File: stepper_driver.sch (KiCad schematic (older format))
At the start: 51 parts, among them IC1 TMC2590-TA-Trinamic, J1 BARREL_JACK, J2 Screw_Terminal_01x04, J3 CONN_01X14, J9 USB_C_Receptacle_USB2.0, Q1 Q_NPN_BEC, Q2 NCE4614, Q3 NCE4614, Q4 Q_NPN_BEC, Q5 NCE4614, Q6 NCE4614, SW1 SW_Push, U1 CH340G, U2 XC6210B332MR, U3 XL1509-5.0, U4 ESP32-WROOM-32, U6 SN74LV1T34DBV, Y1 12MHz

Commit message: Added PCB v1
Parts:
- C8: value 1uF/50V -> 1uF; footprint Capacitor_SMD:C_0603_1608Metric -> Capacitor_SMD:C_0402_1005Metric; LCSC C15849 -> C52923
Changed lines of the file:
@@
 Wire Wire Line
 	5200 1800 5350 1800
-Text Label 6700 1800 0    50   ~ 0
+Text Label 6700 1800 0    60   ~ 0
 IO0
 Wire Wire Line
@@
 Wire Wire Line
 	1050 8450 1050 8350
-$Comp
-L Device:C C8
-U 1 1 61C15625
-P 1050 8850
-F 0 "C8" H 1165 8896 50  0000 L CNN
-F 1 "1uF/50V" H 900 8750 50  0000 L CNN
-F 2 "Capacitor_SMD:C_0603_1608Metric" H 1088 8700 50  0001 C CNN
-F 3 "~" H 1050 8850 50  0001 C CNN
-F 4 "C15849" H 1050 8850 50  0001 C CNN "LCSC"
-	1    1050 8850
-	1    0    0    -1
-$EndComp
 Wire Wire Line
 	1050 8700 1050 8650
@@
 Text Label 5300 7950 2    50   ~ 0
 I39
-Text Label 6700 4000 0    50   ~ 0
+Text Label 6700 4000 0    60   ~ 0
 I34
-Text Label 6700 4100 0    50   ~ 0
+Text Label 6700 4100 0    60   ~ 0
 I35
 Text Label 5300 8050 2    50   ~ 0
@@
 Text Label 5300 8150 2    50   ~ 0
 I35
-Text Label 6700 3800 0    50   ~ 0
+Text Label 6700 3800 0    60   ~ 0
 IO32
-Text Label 6700 3900 0    50   ~ 0
+Text Label 6700 3900 0    60   ~ 0
 IO33
 Text Label 5300 8250 2    50   ~ 0
@@
 Wire Wire Line
 	5150 7750 5300 7750
-Text Label 6700 2500 0    50   ~ 0
+Text Label 6700 2500 0    60   ~ 0
 IO13
-Text Label 6700 3300 0    50   ~ 0
+Text Label 6700 3300 0    60   ~ 0
 IO22
 Text Label 5300 8450 2    50   ~ 0
 IO22
-Text Label 6700 2800 0    50   ~ 0
+Text Label 6700 2800 0    60   ~ 0
 IO16
-Text Label 6700 2900 0    50   ~ 0
+Text Label 6700 2900 0    60   ~ 0
 IO17
 Wire Wire Line
@@
 Text Label 5300 8550 2    50   ~ 0
 IO17
-Text Label 6700 2000 0    50   ~ 0
+Text Label 6700 2000 0    60   ~ 0
 IO2
-Text Label 6700 2700 0    50   ~ 0
+Text Label 6700 2700 0    60   ~ 0
 IO15
 Text Label 5300 8750 2    50   ~ 0
@@
 	1    0    0    -1
 $EndComp
+$Comp
+L Device:C C?
+U 1 1 617F308D
+P 1050 8850
+AR Path="/5F1ED570/617F308D" Ref="C?"  Part="1"
+AR Path="/617F308D" Ref="C8"  Part="1"
+F 0 "C8" H 950 8950 50  0000 L CNN
+F 1 "1uF" H 850 8750 50  0000 L CNN
+F 2 "Capacitor_SMD:C_0402_1005Metric" H 1088 8700 50  0001 C CNN
+F 3 "~" H 1050 8850 50  0001 C CNN
+F 4 "C52923" H 1050 8850 50  0001 C CNN "LCSC"
+	1    1050 8850
+	1    0    0    -1
+$EndComp

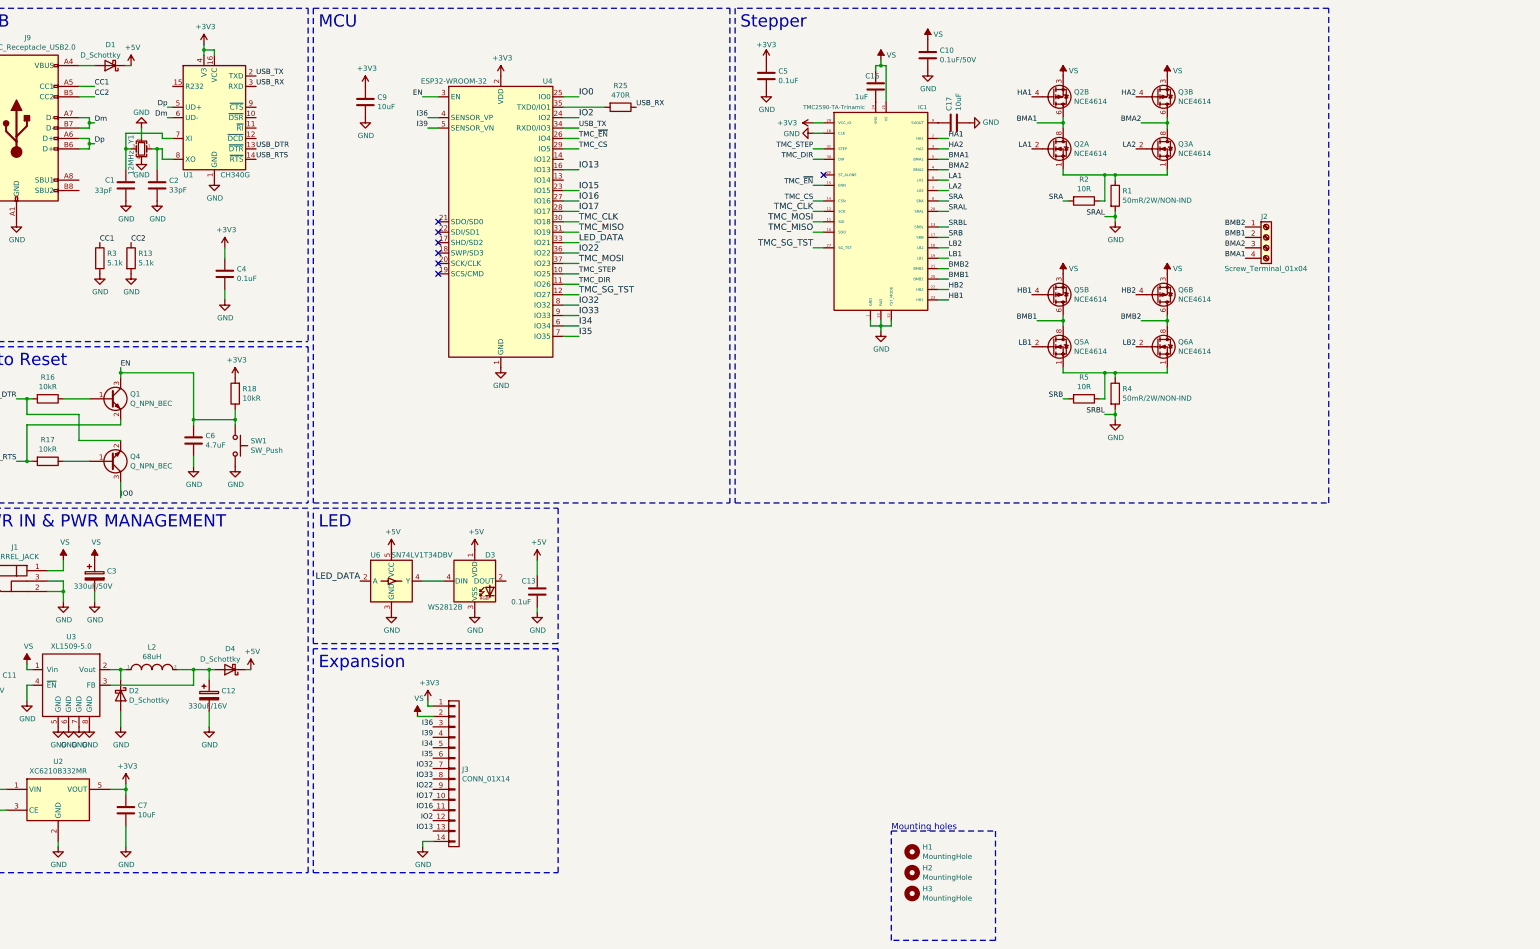
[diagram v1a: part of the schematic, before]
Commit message: Hardware design v2 with TMC2160 driver and NEMA 23 form factor for mounting
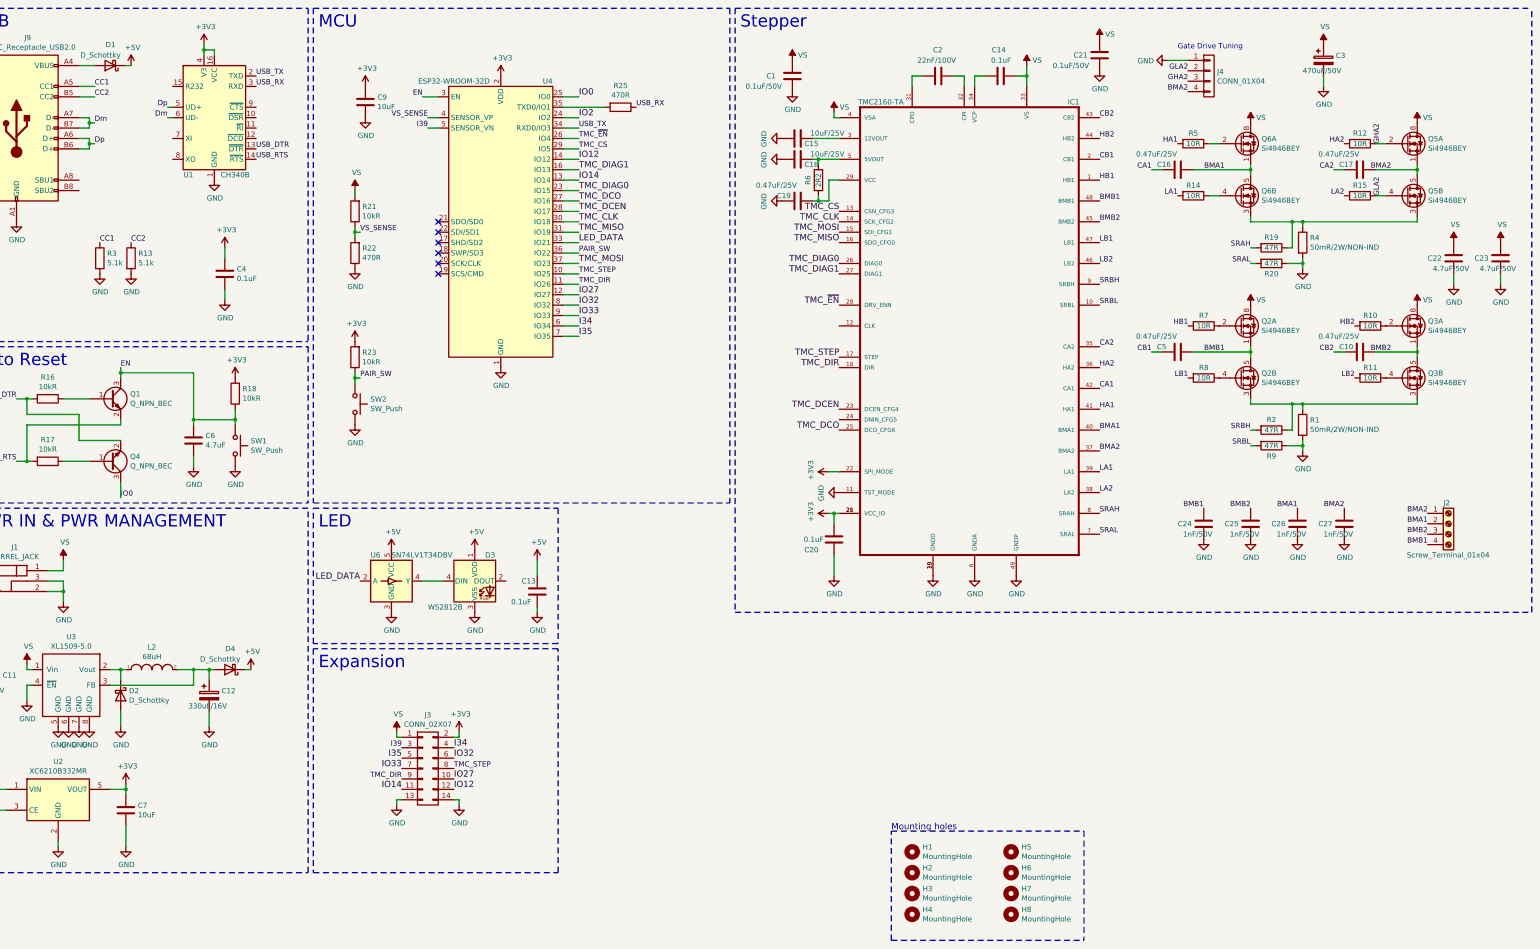
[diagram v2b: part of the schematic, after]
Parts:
- removed IC1: TMC2590-TA-Trinamic, TMC2590-eval:TQFP32-5x5mm, symbol tmc2590-ta-trinamic:TMC2590-TA-Trinamic
- removed J3: CONN_01X14, Connector_PinHeader_2.54mm:PinHeader_1x14_P2.54mm_Vertical, symbol conn1:CONN_01X14
- removed Q2, Q3, Q5, Q6: NCE4614, Package_SO:SOIC-8_3.9x4.9mm_P1.27mm, symbol Transistor_FET:IRF7309IPBF
- removed Y1: 12MHz, Crystal:Crystal_SMD_2520-4Pin_2.5x2.0mm, symbol Device:Crystal_GND24_Small
- added C14, C20: 0.1uF, Capacitor_SMD:C_0402_1005Metric, symbol Device:C
- added C15, C18: 10uF/25V, Capacitor_SMD:C_0603_1608Metric, symbol Device:C
- added C19: 0.47uF/25V, Capacitor_SMD:C_0402_1005Metric, symbol Device:C
- added C21: 0.1uF/50V, Capacitor_SMD:C_0603_1608Metric, symbol Device:C
- added C22, C23: 4.7uF/50V, Capacitor_SMD:C_0805_2012Metric, symbol Device:C
- added C24, C25, C26, C27: 1nF/50V, Capacitor_SMD:C_0402_1005Metric, symbol Device:C
- added H4, H5, H6, H7, H8: MountingHole, MountingHole:MountingHole_3.5mm, symbol Mechanical:MountingHole
- added IC1: TMC2160-TA, Package_QFP:LQFP-48-1EP_7x7mm_P0.5mm_EP3.6x3.6mm_ThermalVias, symbol TMC2160-TA:TMC2160-TA
- added J3: CONN_02X07, Connector_PinHeader_2.54mm:PinHeader_2x07_P2.54mm_Vertical, symbol conn1:CONN_02X07
- added J4: CONN_01X04, Connector_PinHeader_1.27mm:PinHeader_1x04_P1.27mm_Vertical, symbol conn1:CONN_01X04
- added Q2, Q3, Q5, Q6: Si4946BEY, Package_SO:SOIC-8_3.9x4.9mm_P1.27mm, symbol Transistor_FET:FDS6890A
- added R10, R11, R12, R14, R15, R7, R8: 10R, Resistor_SMD:R_0402_1005Metric, symbol Device:R
- added R19, R20, R9: 47R, Resistor_SMD:R_0402_1005Metric, symbol Device:R
- added R21, R23: 10kR, Resistor_SMD:R_0402_1005Metric, symbol Device:R
- added R22: 470R, Resistor_SMD:R_0402_1005Metric, symbol Device:R
- added R6: 2R2, Resistor_SMD:R_0402_1005Metric, symbol Device:R
- added SW2: SW_Push, Switch:SW_Push_1P1T_NO_5.1x5.1mm, symbol Switch:SW_Push
- C1: value 33pF -> 0.1uF/50V; footprint Capacitor_SMD:C_0402_1005Metric -> Capacitor_SMD:C_0603_1608Metric; LCSC C1562 -> C14663
- C10: value 0.1uF/50V -> 0.47uF/25V; footprint Capacitor_SMD:C_0603_1608Metric -> Capacitor_SMD:C_0402_1005Metric; LCSC C14663 -> C437527
- C16: value 1uF -> 0.47uF/25V; LCSC C52923 -> C437527
- C17: value 10uF -> 0.47uF/25V; LCSC C15525 -> C437527
- C2: value 33pF -> 22nF/100V; footprint Capacitor_SMD:C_0402_1005Metric -> Capacitor_SMD:C_0603_1608Metric; LCSC C1562 -> C342519
- C3: value 330uF/50V -> 470uF/50V; LCSC C88733 -> C106526
- C5: value 0.1uF -> 0.47uF/25V; LCSC C1525 -> C437527
- H1, H2, H3: footprint MountingHole:MountingHole_3.2mm_M3 -> MountingHole:MountingHole_3.5mm
- J2: footprint TerminalBlock_Phoenix:TerminalBlock_Phoenix_MPT-0,5-4-2.54_1x04_P2.54mm_Horizontal -> cixi_kefa_screw_terminals:KF2EDGR-3.81-4P; LCSC C474922 -> C441184
- R2: value 10R -> 47R; LCSC C25077 -> C25118
- U1: value CH340G -> CH340B; LCSC C14267 -> C81010
- U4: value ESP32-WROOM-32 -> ESP32-WROOM-32D; LCSC C82899 -> C473012
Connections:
- net SRB is gone; now on net HA1: R5.2
- net +3V3: now also C20.2, IC1.20 (VCC_IO), IC1.21 (VCC_IO), IC1.22 (SPI_MODE), J3.2 (P2), R23.2; no longer C5.1
- net BMA1: now also C16.1, J2.2 (Pin_2), C26.1, IC1.40 (BMA1), Q6.1 (S1), Q6.5 (D2), Q6.6 (D2); no longer J2.4 (Pin_4)
- net BMA2: now also C17.1, J2.1 (Pin_1), C27.1, IC1.37 (BMA2), J4.4 (P4), Q5.1 (S1), Q5.5 (D2), Q5.6 (D2); no longer J2.3 (Pin_3)
- net BMB1: now also C5.1, J2.4 (Pin_4), C24.1, IC1.48 (BMB1), Q2.1 (S1), Q2.5 (D2), Q2.6 (D2); no longer J2.2 (Pin_2)
- net BMB2: now also C10.1, J2.3 (Pin_3), C25.1, IC1.45 (BMB2), Q3.1 (S1), Q3.5 (D2), Q3.6 (D2); no longer J2.1 (Pin_1)
- net GND: now also C15.1, C18.1, C19.2, C20.1, C21.2, C22.2, C23.2, C24.2, C25.2, C26.2, C27.2, IC1.11 (TST_MODE), IC1.19 (GNDD), IC1.30 (GNDD), IC1.49 (GNDP), IC1.6 (GNDA), J3.13 (P13), J3.14 (P14), J4.1 (P1), R20.1, R22.1, R9.1, SW2.2; no longer C10.2, C17.2, C2.2, C5.2
- net HA1: now also IC1.41 (HA1)
- net HA2: now also IC1.36 (HA2), R12.2
- net HB1: now also IC1.1 (HB1), R7.2
- net HB2: now also IC1.44 (HB2), R10.2
- net I34: now also J3.4 (P4)
- net I35: now also J3.5 (P5)
- net I39: now also J3.3 (P3)
- net IO32: now also J3.6 (P6)
- net IO33: now also J3.7 (P7)
- net LA1: now also IC1.39 (LA1), R14.2
- net LA2: now also IC1.38 (LA2), R15.2
- net LB1: now also IC1.47 (LB1), R8.2
- net LB2: now also IC1.46 (LB2), R11.2
- net TMC_CLK: now also IC1.14 (SCK_CFG2)
- net TMC_CS: now also IC1.13 (CSN_CFG3)
- net TMC_DIR: now also IC1.18 (DIR), J3.9 (P9)
- net TMC_MISO: now also IC1.16 (SDO_CFG0)
- net TMC_MOSI: now also IC1.15 (SDI_CFG1)
- net TMC_STEP: now also IC1.17 (STEP), J3.8 (P8)
- net TMC_~EN: now also IC1.28 (DRV_ENN)
- net VS: now also C1.1, C14.2, C21.1, C22.1, C23.1, IC1.33 (VS), IC1.4 (VSA), J3.1 (P1), Q2.7 (D1), Q2.8 (D1), Q3.7 (D1), Q3.8 (D1), Q5.7 (D1), Q5.8 (D1), Q6.7 (D1), Q6.8 (D1), R21.2; no longer C10.1, C16.1
- net IO14: now reaches U4.13 (IO14)
- net IO14: now also J3.11 (P11)
- net IO12: now reaches U4.14 (IO12)
- net IO12: now also J3.12 (P12)
- net at U1.7 (XI): no longer C1.1
- net at U1.8 (XO): no longer C2.1
- net at R1.1, R2.1: now also Q2.3 (S2), Q3.3 (S2)
- net CA1: now reaches C16.2
- net CA1: now also IC1.42 (CA1)
- net at R4.1: now also Q5.3 (S2), Q6.3 (S2), R19.1; no longer R5.1
- net I36 renamed VS_SENSE
- net VS_SENSE: now also R21.1, R22.2
- net IO13 renamed TMC_DIAG1
- net TMC_DIAG1: now also IC1.27 (DIAG1)
- net IO15 renamed TMC_DIAG0
- net TMC_DIAG0: now also IC1.26 (DIAG0)
- net IO16 renamed TMC_DCO
- net TMC_DCO: now also IC1.25 (DCO_CFG6)
- net IO17 renamed TMC_DCEN
- net TMC_DCEN: now also IC1.23 (DCEN_CFG4)
- net IO22 renamed PAIR_SW
- net PAIR_SW: now also R23.1, SW2.1
- net SRA renamed SRBH
- net SRBH: now also IC1.9 (SRBH)
- net TMC_SG_TST renamed IO27
- net IO27: now also J3.10 (P10)
- new net: Q2.2 (G1), R7.1
- new net: Q3.2 (G1), R10.1
- new net: Q2.4 (G2), R8.1
- new net: Q3.4 (G2), R11.1
- new net: C19.1, IC1.29 (VCC), R6.1
- new net: C15.2, IC1.3 (12VOUT)
- new net: C2.2, IC1.31 (CPO)
- new net: C2.1, IC1.32 (CPI)
- new net: C14.1, IC1.34 (VCP)
- new net: C18.2, IC1.5 (5VOUT), R6.2
- new net: Q6.2 (G1), R5.1
- new net: Q6.4 (G2), R14.1
- new net CA2: C17.2, IC1.35 (CA2)
- new net CB1: C5.2, IC1.2 (CB1)
- new net CB2: C10.2, IC1.43 (CB2)
- new net GHA2: J4.3 (P3), Q5.2 (G1), R12.1
- new net GLA2: J4.2 (P2), Q5.4 (G2), R15.1
- new net SRAH: IC1.8 (SRAH), R19.2
- new net SRAL: IC1.7 (SRAL), R20.2
- new net SRBL: IC1.10 (SRBL), R9.2
- no-connect marks 7 -> 6
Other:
- note added: "Gate Drive Tuning"
- moved on the sheet: C3, J2, R1, R2

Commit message: Minor board updates
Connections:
- net GND: now also IC1.12 (CLK)
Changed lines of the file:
@@
 Text Label 7250 1900 0    50   ~ 0
 USB_RX
-Text Label 6700 2100 0    50   ~ 0
-USB_TX
 $Comp
 L Switch:SW_Push SW?
@@
 Wire Notes Line
 	4150 950  8150 950
-Text Label 6700 3200 0    60   ~ 0
+Text Label 6700 3200 0    50   ~ 0
 LED_DATA
-Text Label 6700 3400 0    60   ~ 0
+Text Label 6700 3400 0    50   ~ 0
 TMC_MOSI
 $Comp
@@
 Wire Wire Line
 	5200 1800 5350 1800
-Text Label 6700 1800 0    60   ~ 0
+Text Label 6700 1800 0    50   ~ 0
 IO0
 Wire Wire Line
@@
 Wire Wire Line
 	6550 1900 6950 1900
-Text Label 6700 2300 0    50   ~ 0
-TMC_CS
 Wire Wire Line
 	6550 4100 6700 4100
@@
 	1    0    0    -1
 $EndComp
-Text Label 9200 3800 2    60   ~ 0
+Text Label 9200 3800 2    50   ~ 0
 TMC_~EN
 $Comp
@@
 	1    0    0    -1
 $EndComp
-Text Label 6700 3100 0    60   ~ 0
-TMC_MISO
-Text Label 6700 3000 0    60   ~ 0
+Text Label 9200 2900 2    50   ~ 0
+TMC_CS
+Text Label 9200 3000 2    50   ~ 0
 TMC_CLK
-Text Label 9200 2900 2    60   ~ 0
-TMC_CS
-Text Label 6700 2200 0    50   ~ 0
-TMC_~EN
-Text Label 9200 3000 2    60   ~ 0
-TMC_CLK
-Text Label 9200 3100 2    60   ~ 0
+Text Label 9200 3100 2    50   ~ 0
 TMC_MOSI
-Text Label 9200 3200 2    60   ~ 0
+Text Label 9200 3200 2    50   ~ 0
 TMC_MISO
 Text Label 12550 4000 2    50   ~ 0
@@
 Text Label 14850 5800 2    50   ~ 0
 BMA2
-Text Label 6700 3700 0    60   ~ 0
+Text Label 6700 3700 0    50   ~ 0
 IO27
-Text Label 9200 4400 2    60   ~ 0
+Text Label 9200 4400 2    50   ~ 0
 TMC_DIR
 Text Label 6700 3600 0    50   ~ 0
 TMC_DIR
-Text Label 9200 4300 2    60   ~ 0
+Text Label 9200 4300 2    50   ~ 0
 TMC_STEP
 Text Label 6700 3500 0    50   ~ 0
@@
 Text Label 5250 2100 2    50   ~ 0
 I39
-Text Label 6700 4000 0    60   ~ 0
+Text Label 6700 4000 0    50   ~ 0
 I34
-Text Label 6700 4100 0    60   ~ 0
+Text Label 6700 4100 0    50   ~ 0
 I35
-Text Label 6700 3800 0    60   ~ 0
+Text Label 6700 3800 0    50   ~ 0
 IO32
-Text Label 6700 3900 0    60   ~ 0
+Text Label 6700 3900 0    50   ~ 0
 IO33
 Wire Wire Line
@@
 Wire Wire Line
 	6700 2900 6550 2900
-Text Label 6700 2000 0    60   ~ 0
-IO2
 Wire Wire Line
 	6550 1800 6700 1800
@@
 Text Label 5250 2000 2    50   ~ 0
 VS_SENSE
-Text Label 6700 2400 0    60   ~ 0
-IO12
 Wire Wire Line
 	6700 2400 6550 2400
-Text Label 6700 2600 0    60   ~ 0
-IO14
 Wire Wire Line
 	6700 2600 6550 2600
@@
 	1    0    0    -1
 $EndComp
-Text Label 9200 4800 2    60   ~ 0
+Text Label 9200 4800 2    50   ~ 0
 TMC_DCEN
-Text Label 9200 5000 2    60   ~ 0
+Text Label 9200 5000 2    50   ~ 0
 TMC_DCO
-Text Label 6700 2900 0    60   ~ 0
+Text Label 9200 3400 2    50   ~ 0
+TMC_DIAG0
+Text Label 9200 3500 2    50   ~ 0
+TMC_DIAG1
+Wire Notes Line
+	8200 6750 15850 6750
+Wire Notes Line
+	15850 6750 15850 950
+Wire Notes Line
+	8200 950  8200 6750
+Wire Notes Line
+	8200 950  15850 950
+Wire Notes Line
+	11550 8850 11550 9900
+Wire Notes Line
+	9700 8850 11550 8850
+Wire Notes Line
+	9700 9900 11550 9900
+$Comp
+L power:GND #PWR0182
+U 1 1 6277F220
+P 9050 4000
+F 0 "#PWR0182" H 9050 3750 50  0001 C CNN
+F 1 "GND" H 9055 3827 50  0000 C CNN
+F 2 "" H 9050 4000 50  0001 C CNN
+F 3 "" H 9050 4000 50  0001 C CNN
+	1    9050 4000
+	0    1    1    0
+$EndComp
+Wire Wire Line
+	9050 4000 9200 4000
+Text Label 6700 2500 0    50   ~ 0
+TMC_DIAG1
+Text Label 6700 2700 0    50   ~ 0
+TMC_DIAG0
+Text Label 6700 2800 0    50   ~ 0
+TMC_DCO
+Text Label 6700 2900 0    50   ~ 0
 TMC_DCEN
-Text Label 6700 2800 0    60   ~ 0
-TMC_DCO
-Text Label 9200 3400 2    60   ~ 0
-TMC_DIAG0
-Text Label 9200 3500 2    60   ~ 0
-TMC_DIAG1
-Text Label 6700 2700 0    60   ~ 0
-TMC_DIAG0
-Text Label 6700 2500 0    60   ~ 0
-TMC_DIAG1
-Wire Notes Line
-	8200 6750 15850 6750
-Wire Notes Line
-	15850 6750 15850 950
-Wire Notes Line
-	8200 950  8200 6750
-Wire Notes Line
-	8200 950  15850 950
-Wire Notes Line
-	11550 8850 11550 9900
-Wire Notes Line
-	9700 8850 11550 8850
-Wire Notes Line
-	9700 9900 11550 9900
+Text Label 6700 2600 0    50   ~ 0
+IO14
+Text Label 6700 2400 0    50   ~ 0
+IO12
+Text Label 6700 2000 0    50   ~ 0
+IO2
+Text Label 6700 2200 0    50   ~ 0
+TMC_~EN
+Text Label 6700 3000 0    50   ~ 0
+TMC_CLK
+Text Label 6700 3100 0    50   ~ 0
+TMC_MISO
+Text Label 6700 2300 0    50   ~ 0
+TMC_CS
+Text Label 6700 2100 0    50   ~ 0
+USB_TX
 $EndSCHEMATC
